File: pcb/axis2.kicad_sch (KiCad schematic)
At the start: 10 parts, among them J12 Mini v1.0 FEMALE sockets, J22 MOTOR PHASES male 1x3, J32 ENCODER JST-SH 6p, J42 MINI POWER: +12V / GND

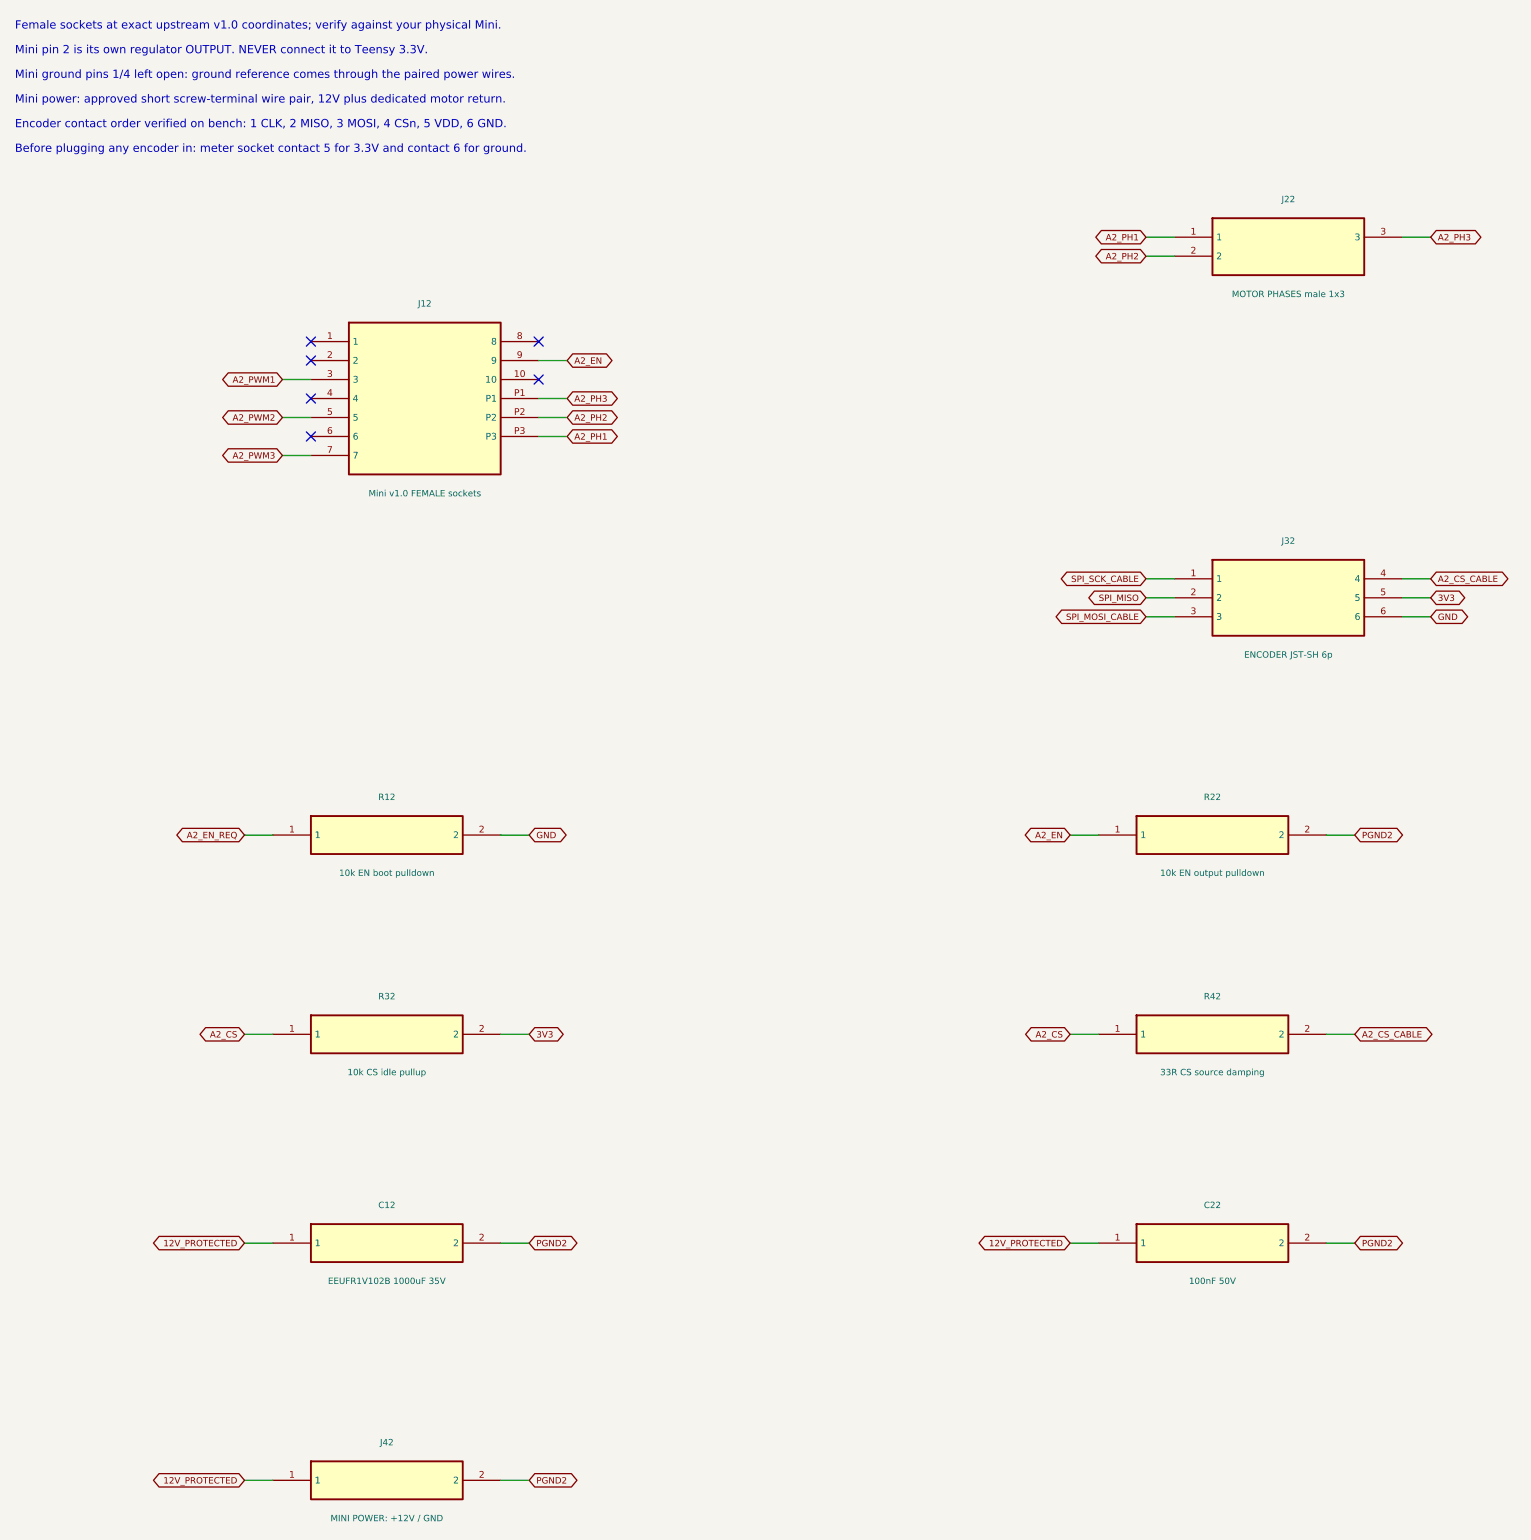
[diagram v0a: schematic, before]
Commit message: feat: finish through-hole six-axis carrier review design
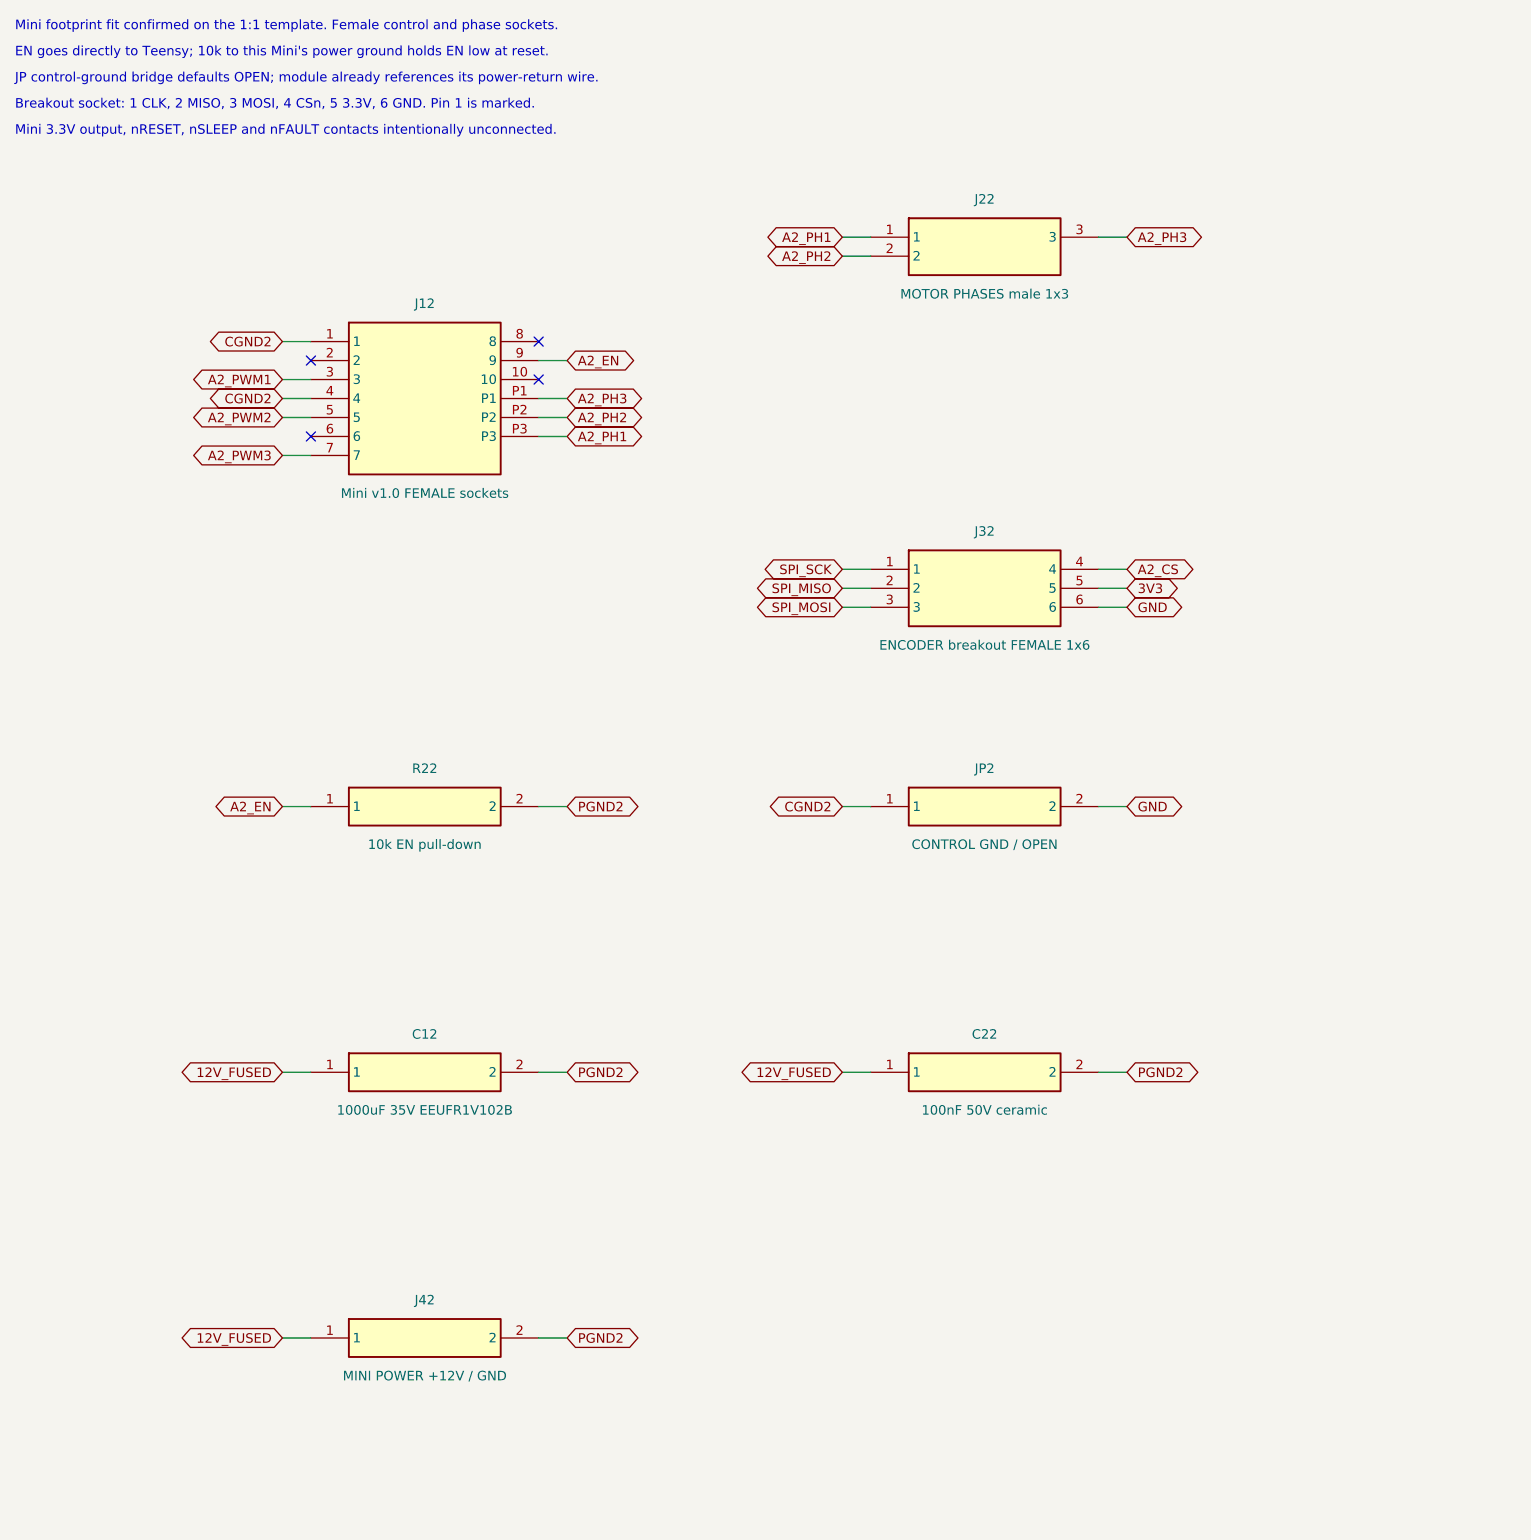
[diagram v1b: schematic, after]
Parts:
- removed R12: 10k EN boot pulldown, Resistor_SMD:R_0603_1608Metric, symbol TrueSkate:R12
- removed R32: 10k CS idle pullup, Resistor_SMD:R_0603_1608Metric, symbol TrueSkate:R32
- removed R42: 33R CS source damping, Resistor_SMD:R_0603_1608Metric, symbol TrueSkate:R42
- added JP2: CONTROL GND / OPEN, TrueSkate:GroundBridge_THT, symbol TrueSkate:JP2
- C12: value EEUFR1V102B 1000uF 35V -> 1000uF 35V EEUFR1V102B; LCSC C128476 -> (none)
- C22: value 100nF 50V -> 100nF 50V ceramic; footprint Capacitor_SMD:C_0603_1608Metric -> Capacitor_THT:C_Disc_D5.0mm_W2.5mm_P5.00mm; LCSC C14663 -> (none)
- J32: value ENCODER JST-SH 6p -> ENCODER breakout FEMALE 1x6; footprint Connector_JST:JST_SH_BM06B-SRSS-TB_1x06-1MP_P1.00mm_Vertical -> Connector_PinSocket_2.54mm:PinSocket_1x06_P2.54mm_Vertical; LCSC C160392 -> (none)
- J42: value MINI POWER: +12V / GND -> MINI POWER +12V / GND
- R22: value 10k EN output pulldown -> 10k EN pull-down; footprint Resistor_SMD:R_0603_1608Metric -> Resistor_THT:R_Axial_DIN0207_L6.3mm_D2.5mm_P7.62mm_Horizontal; LCSC C25804 -> (none)
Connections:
- net A2_CS_CABLE is gone; now on net A2_CS: J32.4
- net GND: now also JP2.2
- net CGND2: now reaches J12.1
- net CGND2: now also J12.4, JP2.1
- net 12V_PROTECTED renamed 12V_FUSED
- net SPI_MOSI_CABLE renamed SPI_MOSI
- net SPI_SCK_CABLE renamed SPI_SCK
- no-connect marks 6 -> 4
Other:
- note added: "Breakout socket: 1 CLK, 2 MISO, 3 MOSI, 4 CSn, 5 3.3V, 6 GND. Pin 1 is marked."
- note added: "EN goes directly to Teensy; 10k to this Mini's power ground holds EN low at reset."
- note added: "JP control-ground bridge defaults OPEN; module already references its power-return wire."
- note added: "Mini 3.3V output, nRESET, nSLEEP and nFAULT contacts intentionally unconnected."
- note added: "Mini footprint fit confirmed on the 1:1 template. Female control and phase sockets."
- note removed: "Before plugging any encoder in: meter socket contact 5 for 3.3V and contact 6 for ground."
- note removed: "Encoder contact order verified on bench: 1 CLK, 2 MISO, 3 MOSI, 4 CSn, 5 VDD, 6 GND."
- note removed: "Female sockets at exact upstream v1.0 coordinates; verify against your physical Mini."
- note removed: "Mini ground pins 1/4 left open: ground reference comes through the paired power wires."
- note removed: "Mini pin 2 is its own regulator OUTPUT. NEVER connect it to Teensy 3.3V."
- note removed: "Mini power: approved short screw-terminal wire pair, 12V plus dedicated motor return."
- title: 04 / Axis 2: index_curl_2 -> 03 / A2: index_curl_2
- moved on the sheet: C12, C22, J22, J32, J42, R22

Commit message: feat: use exact Mini v1.0 footprints with direct power routing
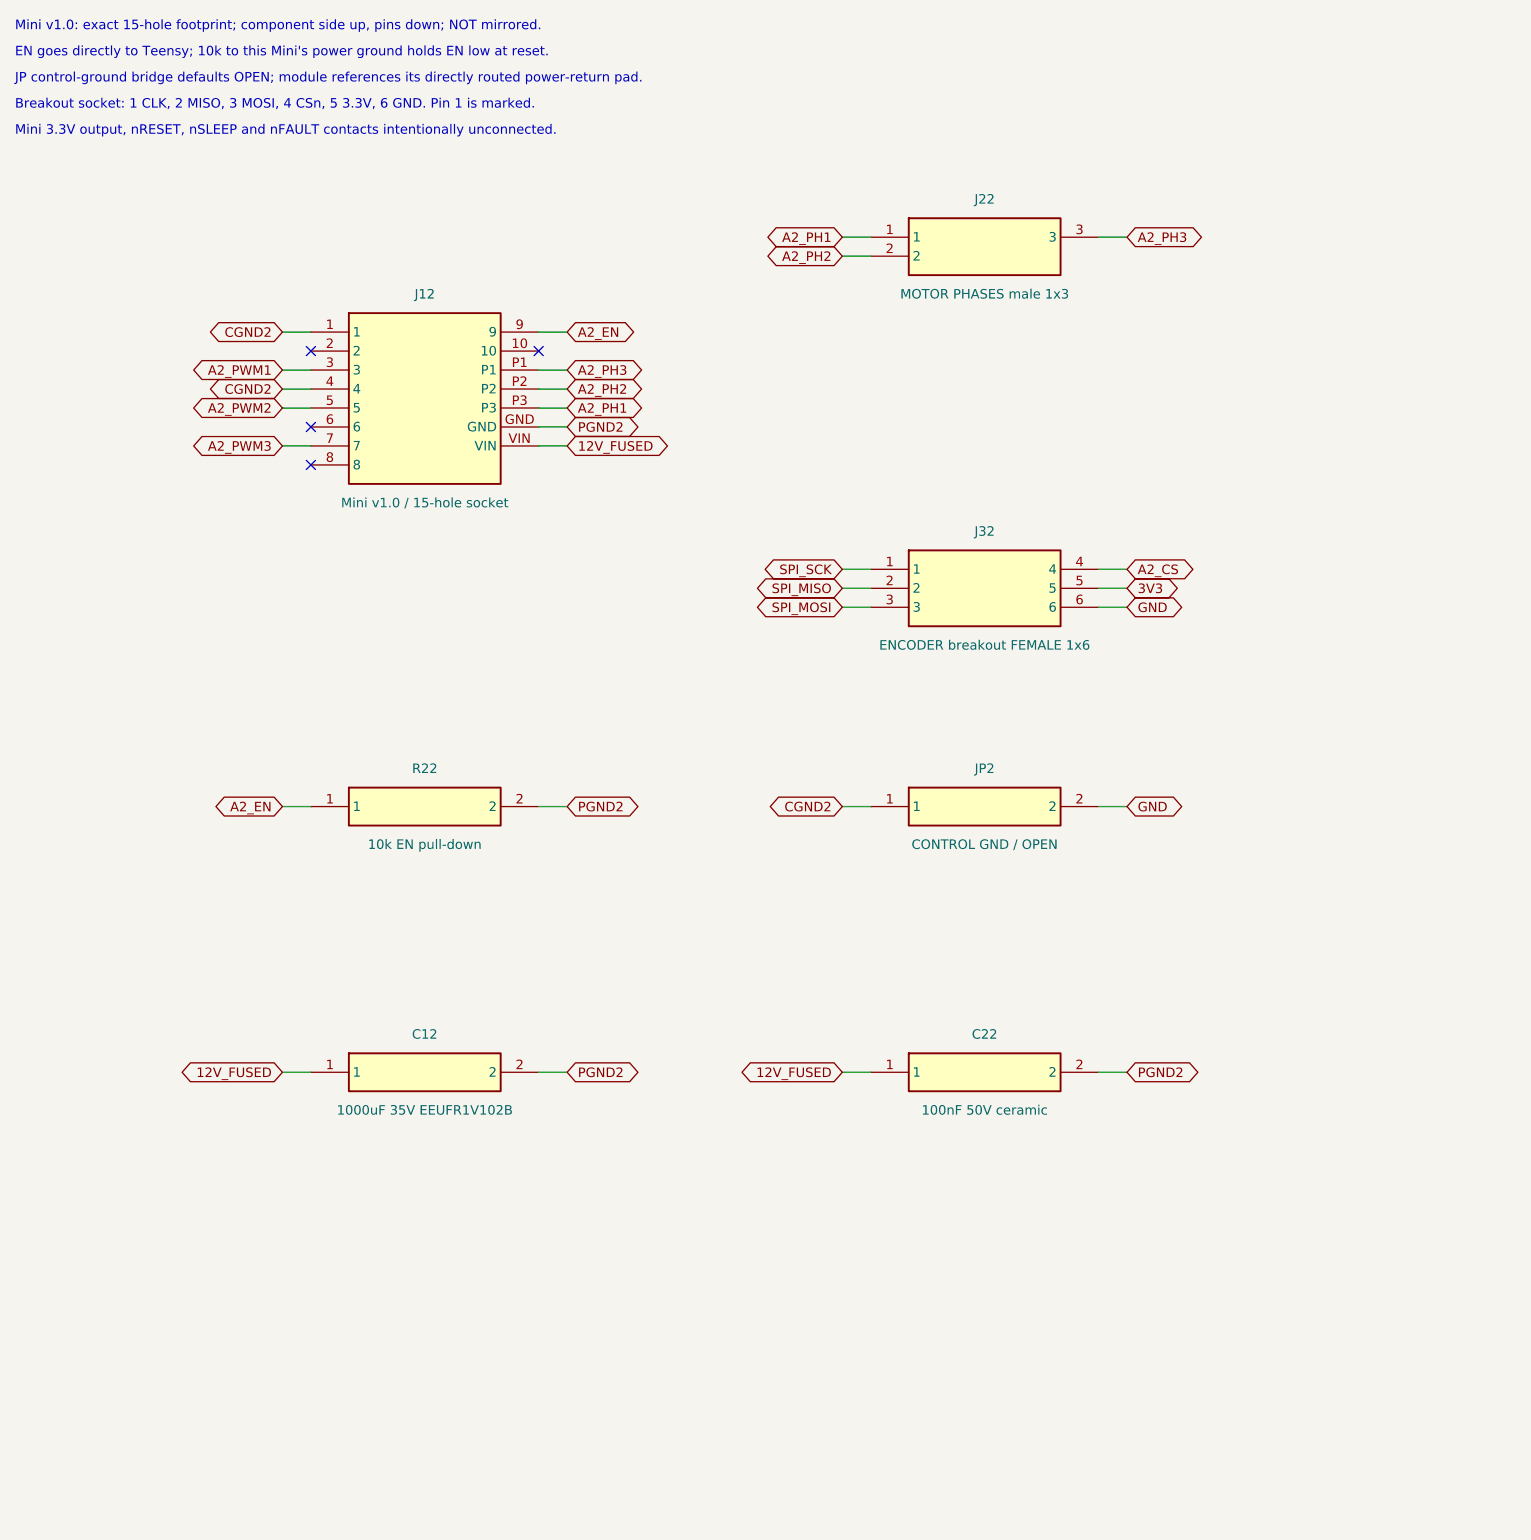
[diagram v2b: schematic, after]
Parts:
- removed J42: MINI POWER +12V / GND, TerminalBlock_Phoenix:TerminalBlock_Phoenix_MKDS-1-2-3.81_1x02_P3.81mm_Horizontal, symbol TrueSkate:J42
- J12: value Mini v1.0 FEMALE sockets -> Mini v1.0 / 15-hole socket; footprint TrueSkate:Mini_v1_Sockets -> TrueSkate:SimpleFOC_Mini_v1.0
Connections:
- net 12V_FUSED: now also J12.VIN
- net PGND2: now also J12.GND
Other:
- note added: "JP control-ground bridge defaults OPEN; module references its directly routed power-return pad."
- note added: "Mini v1.0: exact 15-hole footprint; component side up, pins down; NOT mirrored."
- note removed: "JP control-ground bridge defaults OPEN; module already references its power-return wire."
- note removed: "Mini footprint fit confirmed on the 1:1 template. Female control and phase sockets."
